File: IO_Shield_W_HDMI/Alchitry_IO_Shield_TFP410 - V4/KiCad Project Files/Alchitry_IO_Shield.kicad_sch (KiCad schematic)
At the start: 1 part, among them U0 boardmezzanine_new

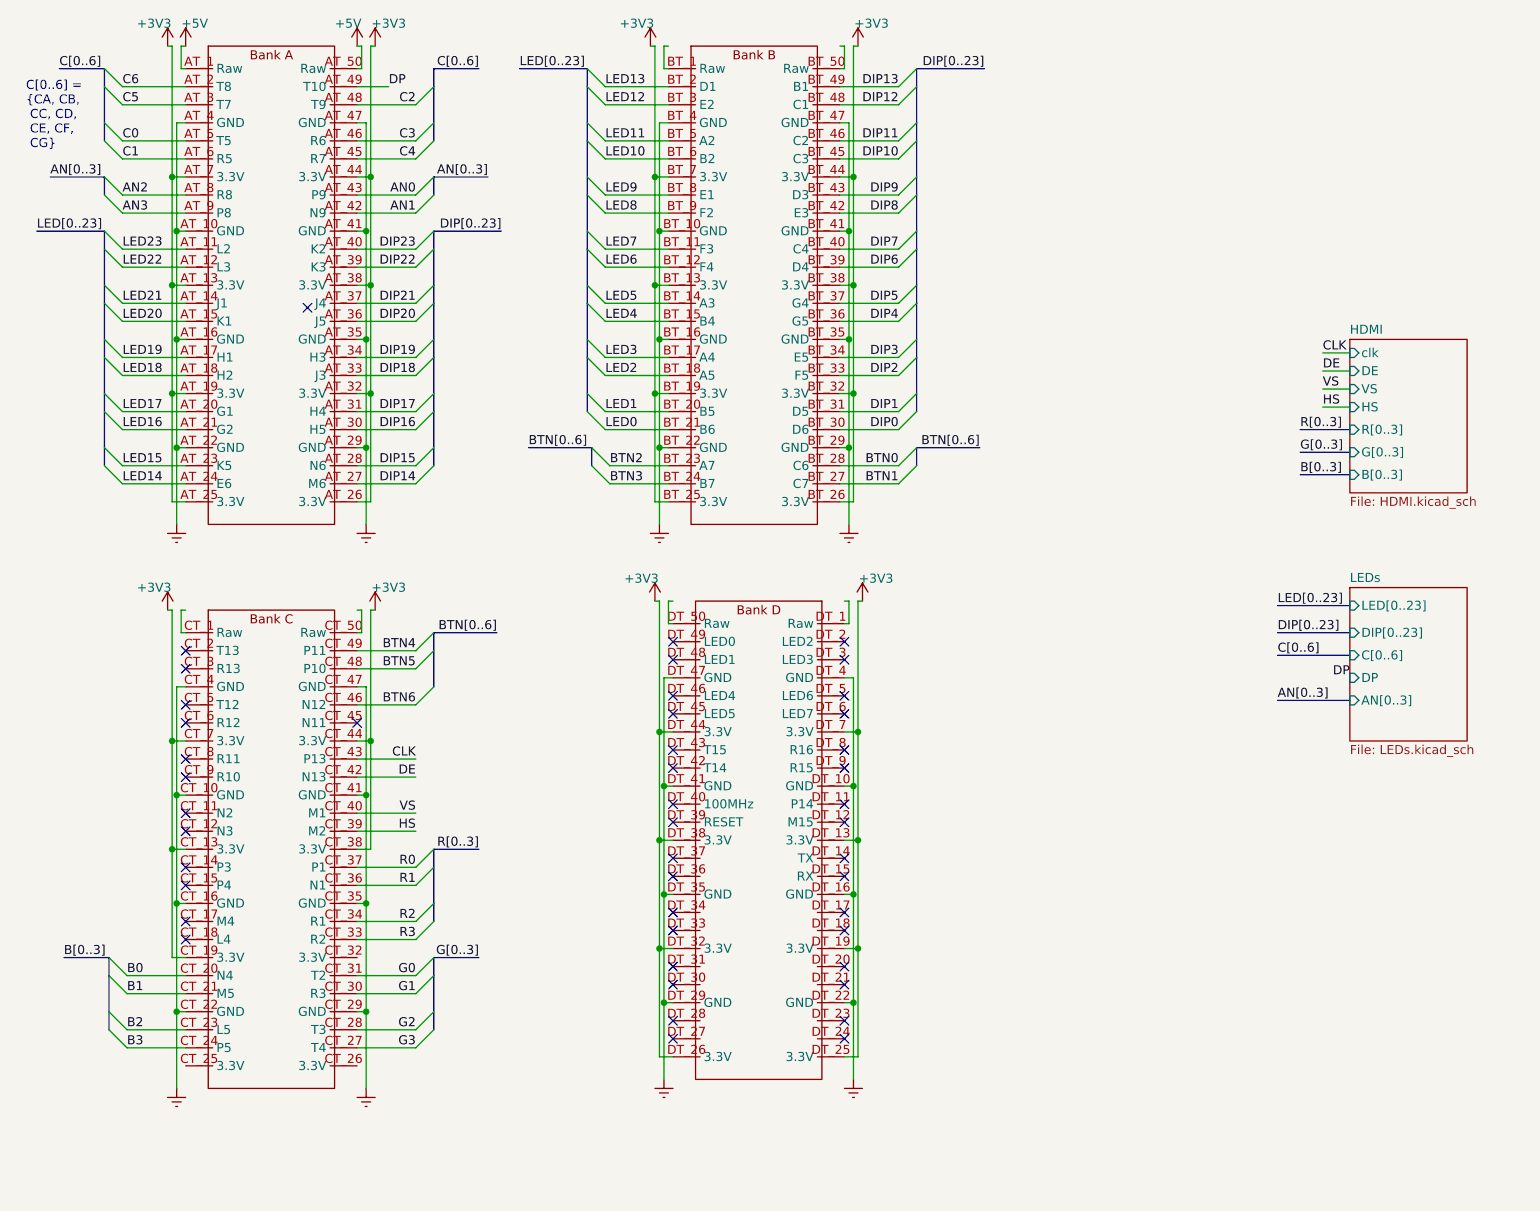
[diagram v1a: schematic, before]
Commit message: updated shield v4 schematic
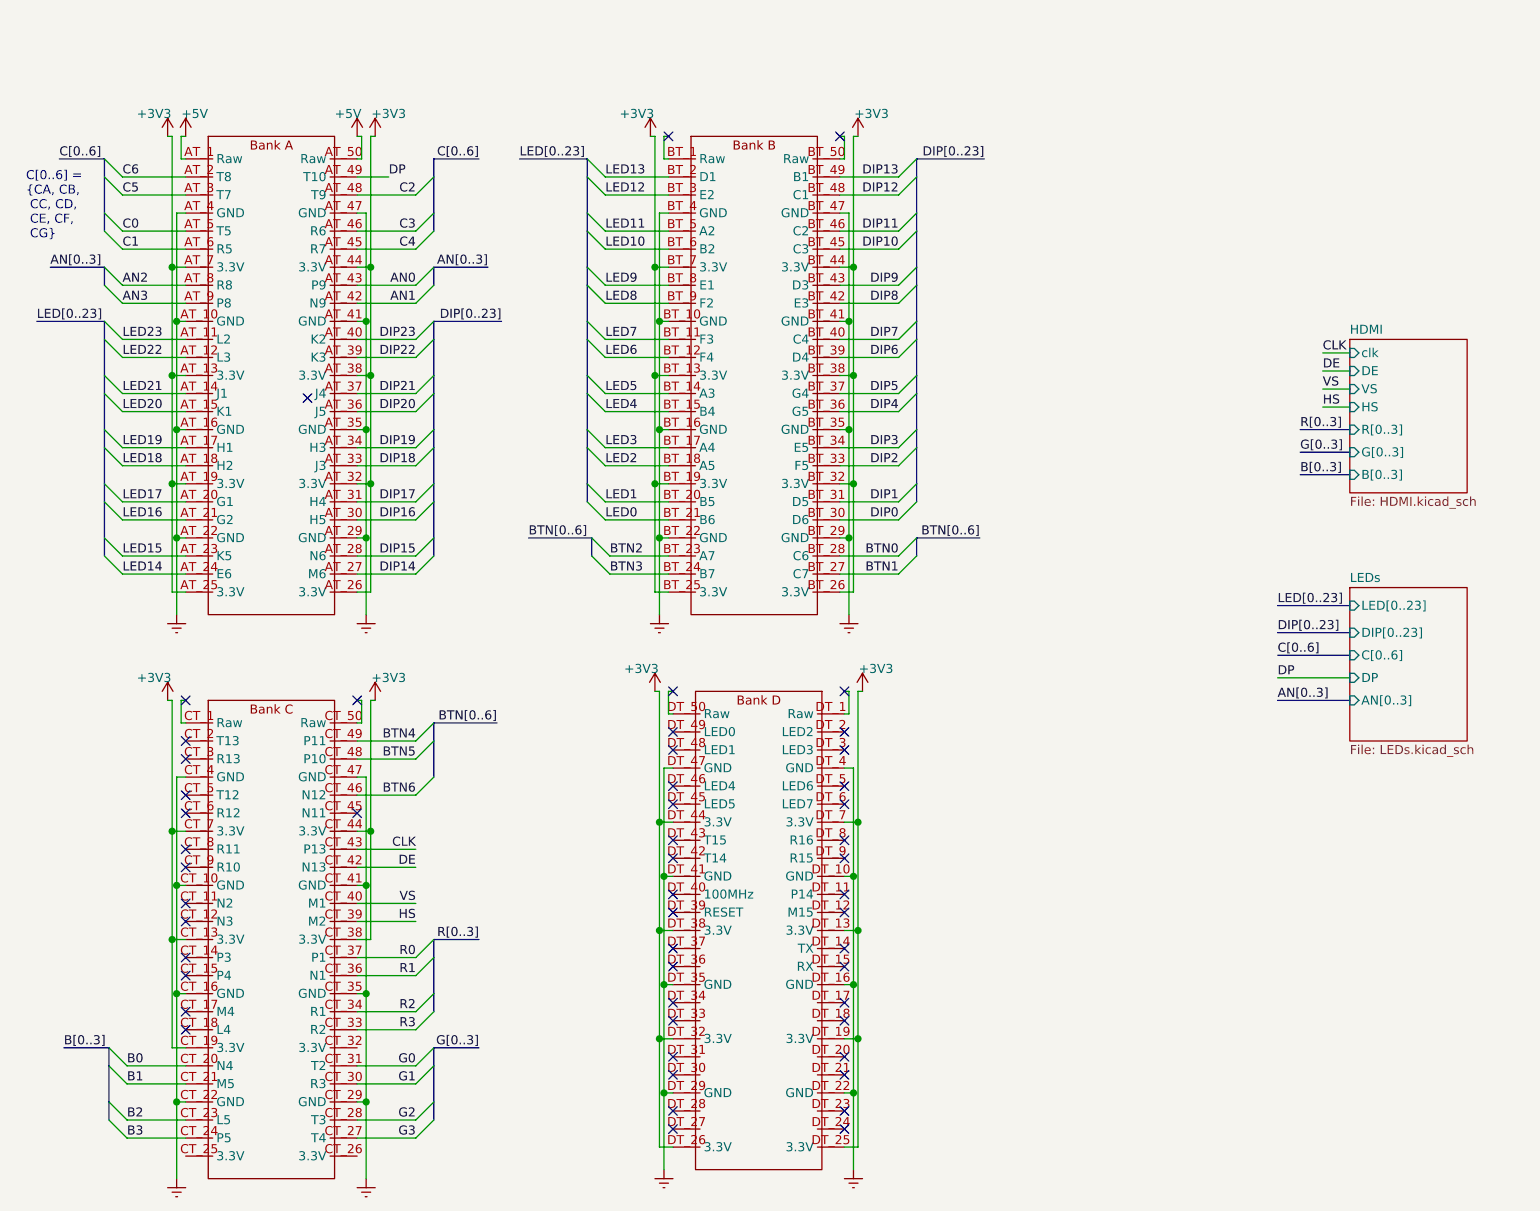
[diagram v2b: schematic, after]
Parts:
- renumbered U0 to U1
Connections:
- no-connect marks 46 -> 52
